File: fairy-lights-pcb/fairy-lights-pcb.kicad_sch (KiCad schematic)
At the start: 5 parts, among them J1 Barrel_Jack_MountingPin, J2 Conn_LED_Strand, U1 WeMos_D1_mini, U2 TXS0108EPW

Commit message: Add board design and missing component footprints
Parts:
- J2: footprint (none) -> Connector_PinHeader_2.54mm:PinHeader_1x04_P2.54mm_Vertical
- R1: footprint (none) -> Resistor_THT:R_Axial_DIN0204_L3.6mm_D1.6mm_P7.62mm_Horizontal
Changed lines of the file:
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@@
 			)
 		)
-		(property "Footprint" ""
+		(property "Footprint" "Connector_PinHeader_2.54mm:PinHeader_1x04_P2.54mm_Vertical"
 			(at 179.07 75.057 0)
 			(effects
@@
 			)
 		)
-		(property "Footprint" ""
+		(property "Footprint" "Resistor_THT:R_Axial_DIN0204_L3.6mm_D1.6mm_P7.62mm_Horizontal"
 			(at 129.54 60.198 90)
 			(effects

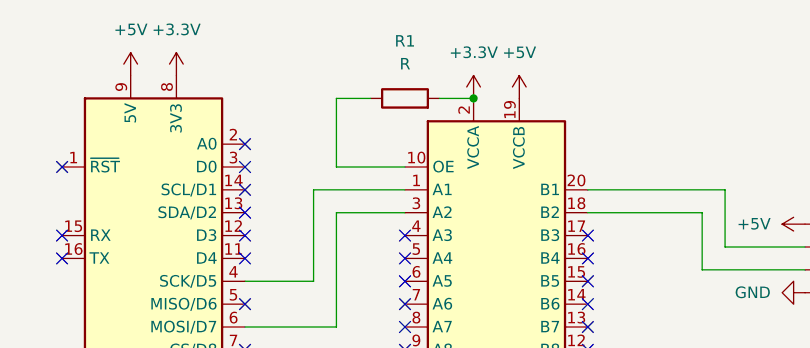
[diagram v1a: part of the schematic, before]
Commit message: Add resistor value and connector annotations
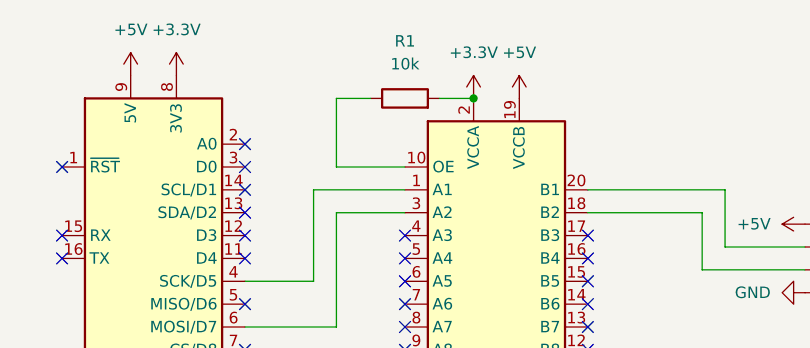
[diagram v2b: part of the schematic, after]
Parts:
- R1: value R -> 10k
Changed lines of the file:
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@@
 			)
 		)
-		(property "Value" "R"
+		(property "Value" "10k"
 			(at 129.54 54.61 90)
 			(effects

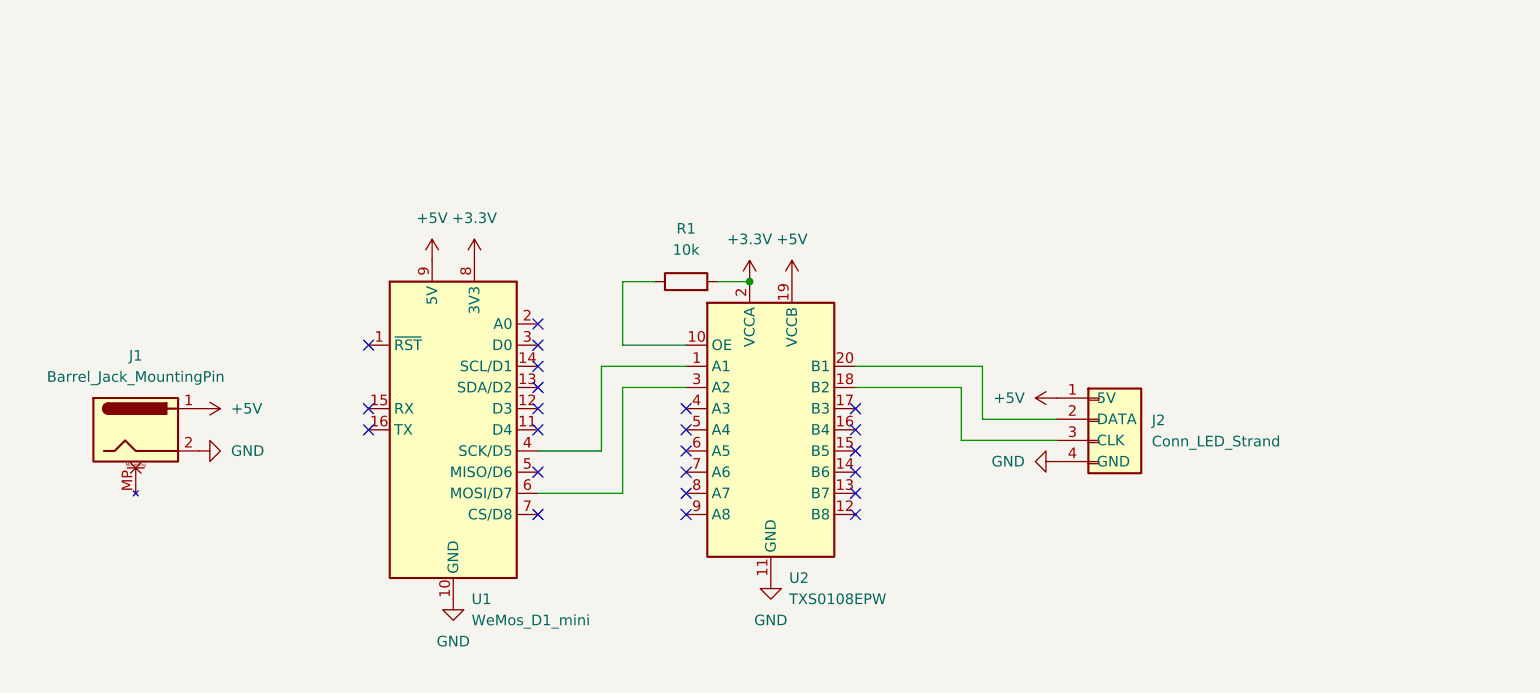
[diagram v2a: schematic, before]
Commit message: Add more stuff
- Two more output headers (functionally identical but one labeled like
  the first LED one and the second generically)
- Header for a power switch (interposed between the power jack and the
  5V rail)
- Header for a user switch/button (from a GPIO pin to ground)
- User LED (from a GPIO pin to ground)
- Miscellaneous header (exposing all other pins of the microcontroller)
- Mounting holes
- Shifted power jack closer to PCB edge
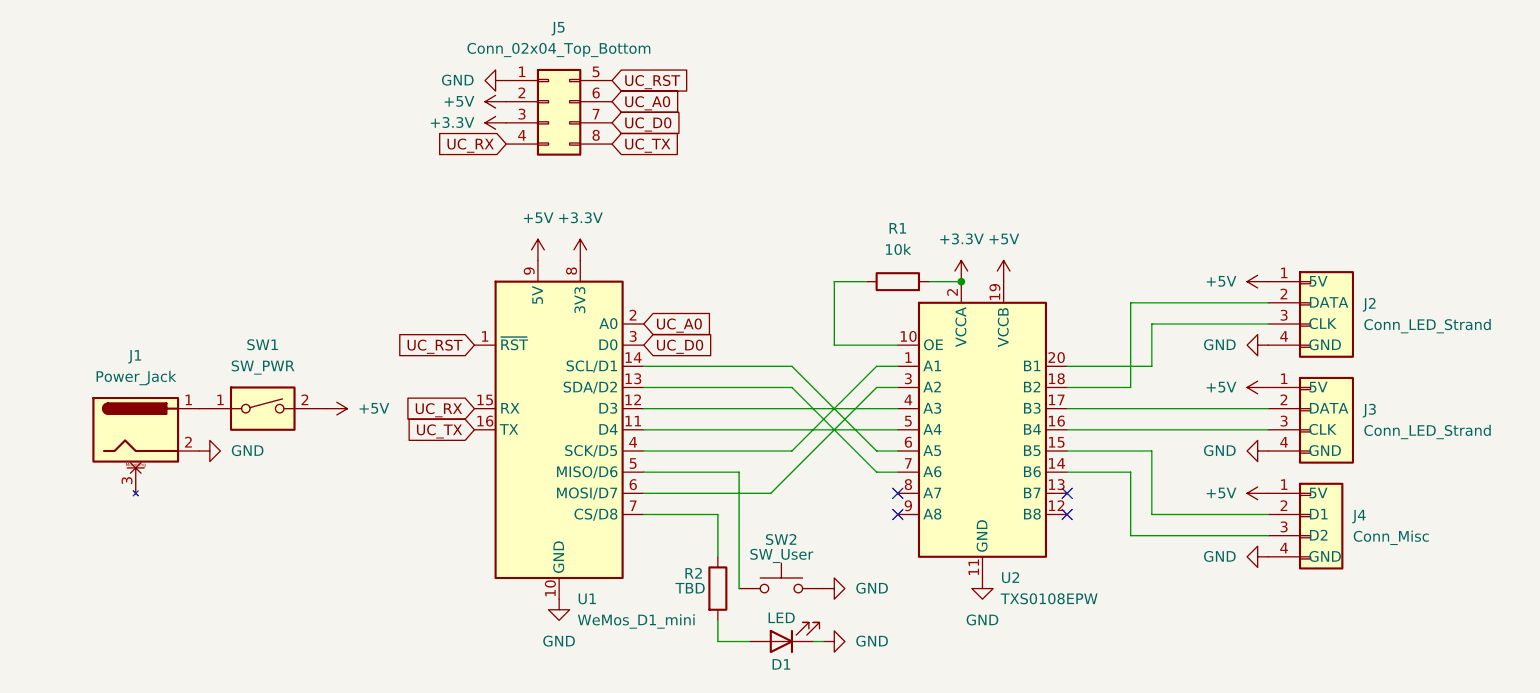
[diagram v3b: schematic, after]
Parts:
- added D1: LED, LED_THT:LED_D3.0mm, symbol Device:LED
- added J3: Conn_LED_Strand, Connector_PinHeader_2.54mm:PinHeader_1x04_P2.54mm_Vertical, symbol CustomSymbols:Conn_LED_Strand
- added J4: Conn_Misc, Connector_PinHeader_2.54mm:PinHeader_1x04_P2.54mm_Vertical, symbol CustomSymbols:Conn_Misc
- added J5: Conn_02x04_Top_Bottom, Connector_PinHeader_2.54mm:PinHeader_2x04_P2.54mm_Vertical, symbol Connector_Generic:Conn_02x04_Top_Bottom
- added R2: TBD, Resistor_THT:R_Axial_DIN0204_L3.6mm_D1.6mm_P7.62mm_Horizontal, symbol Device:R
- added SW1: SW_PWR, Connector_PinHeader_2.54mm:PinHeader_1x02_P2.54mm_Vertical, symbol CustomSymbols:SW_PWR
- added SW2: SW_User, Connector_PinHeader_2.54mm:PinHeader_1x02_P2.54mm_Vertical, symbol Switch:SW_Push
- J1: value Barrel_Jack_MountingPin -> Power_Jack
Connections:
- net +3.3V: now also J5.3 (Pin_3)
- net +5V: now also J3.1 (5V), J4.1 (5V), J5.2 (Pin_2), SW1.2; no longer J1.1
- net GND: now also D1.1 (K), J3.4 (GND), J4.4 (GND), J5.1 (Pin_1), SW2.2
- net at J2.2 (DATA): now also U2.18 (B2); no longer U2.20 (B1)
- net at J2.3 (CLK): now also U2.20 (B1); no longer U2.18 (B2)
- net at U2.14 (B6): now also J4.3 (D2)
- net at U2.15 (B5): now also J4.2 (D1)
- net at U2.16 (B4): now also J3.3 (CLK)
- net at U2.17 (B3): now also J3.2 (DATA)
- net at U2.4 (A3): now also U1.12 (D3)
- net at U2.5 (A4): now also U1.11 (D4)
- net at U2.6 (A5): now also U1.14 (SCL/D1)
- net at U2.7 (A6): now also U1.13 (SDA/D2)
- net UC_RST: now reaches U1.1 (~{RST})
- net UC_RST: now also J5.5 (Pin_5)
- net UC_RX: now reaches U1.15 (RX)
- net UC_RX: now also J5.4 (Pin_4)
- net UC_TX: now reaches U1.16 (TX)
- net UC_TX: now also J5.8 (Pin_8)
- net UC_A0: now reaches U1.2 (A0)
- net UC_A0: now also J5.6 (Pin_6)
- net UC_D0: now reaches U1.3 (D0)
- net UC_D0: now also J5.7 (Pin_7)
- net at U1.5 (MISO/D6): now also SW2.1
- net at U1.7 (CS/D8): now also R2.1
- new net: D1.2 (A), R2.2
- new net: J1.1, SW1.1
- no-connect marks 23 -> 4
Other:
- moved on the sheet: J2, R1, U1, U2

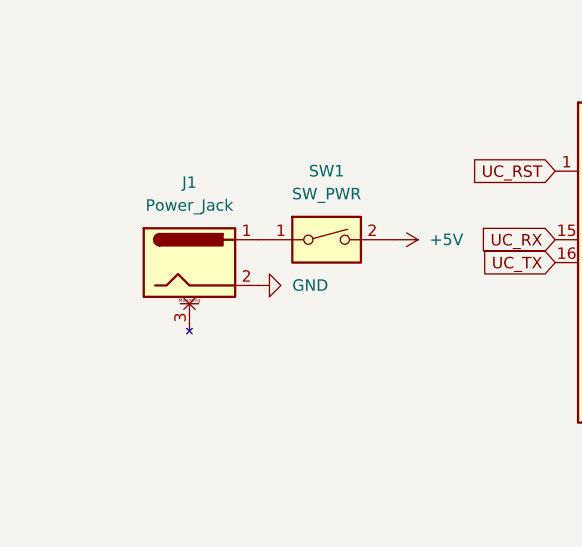
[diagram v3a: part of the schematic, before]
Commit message: Increase thickness of 5V traces
Also redoes all routing, because why not.
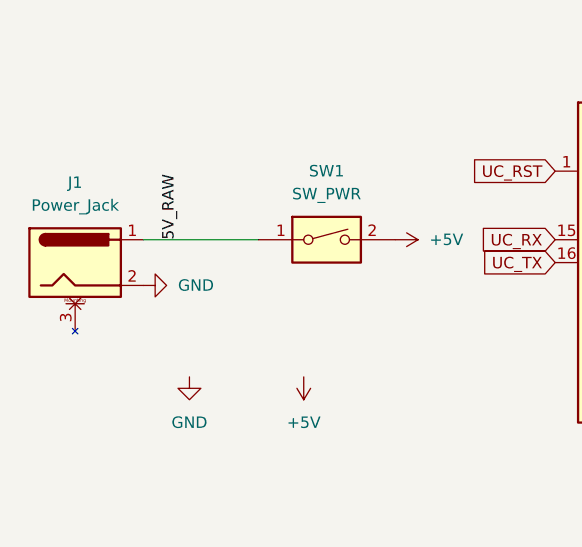
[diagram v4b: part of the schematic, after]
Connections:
- net 5V_RAW: now reaches J1.1, SW1.1
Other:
- moved on the sheet: J1
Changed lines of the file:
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@@
+	(wire
+		(pts
+			(xy 58.42 73.66) (xy 71.12 73.66)
+		)
+		(stroke
+			(width 0)
+			(type default)
+		)
+	)
 	(wire
 		(pts
@@
 		)
 	)
+	(label "5V_RAW"
+		(at 62.23 73.66 90)
+		(fields_autoplaced yes)
+		(effects
+			(font
+				(size 1.27 1.27)
+			)
+			(justify left bottom)
+		)
+	)
 	(global_label "UC_D0"
 		(shape input)
@@
 		)
 	)
+	(netclass_flag ""
+		(length 2.54)
+		(shape round)
+		(at 63.5 88.9 0)
+		(fields_autoplaced yes)
+		(effects
+			(font
+				(size 1.27 1.27)
+			)
+			(justify left bottom)
+		)
+		(property "Netclass" "Power"
+			(at 64.1985 86.36 0)
+			(effects
+				(font
+					(size 1.27 1.27)
+					(italic yes)
+				)
+				(justify left)
+			)
+		)
+	)
+	(netclass_flag ""
+		(length 2.54)
+		(shape round)
+		(at 64.77 73.66 0)
+		(fields_autoplaced yes)
+		(effects
+			(font
+				(size 1.27 1.27)
+			)
+			(justify left bottom)
+		)
+		(property "Netclass" "Power"
+			(at 65.4685 71.12 0)
+			(effects
+				(font
+					(size 1.27 1.27)
+					(italic yes)
+				)
+				(justify left)
+			)
+		)
+	)
+	(netclass_flag ""
+		(length 2.54)
+		(shape round)
+		(at 76.2 88.9 0)
+		(fields_autoplaced yes)
+		(effects
+			(font
+				(size 1.27 1.27)
+			)
+			(justify left bottom)
+		)
+		(property "Netclass" "Power"
+			(at 76.8985 86.36 0)
+			(effects
+				(font
+					(size 1.27 1.27)
+					(italic yes)
+				)
+				(justify left)
+			)
+		)
+	)
 	(symbol
 		(lib_id "Switch:SW_Push")
@@
 	)
 	(symbol
+		(lib_id "power:GND")
+		(at 63.5 88.9 0)
+		(unit 1)
+		(exclude_from_sim no)
+		(in_bom yes)
+		(on_board yes)
+		(dnp no)
+		(fields_autoplaced yes)
+		(property "Reference" "#PWR021"
+			(at 63.5 95.25 0)
+			(effects
+				(font
+					(size 1.27 1.27)
+				)
+				(hide yes)
+			)
+		)
+		(property "Value" "GND"
+			(at 63.5 93.98 0)
+			(effects
+				(font
+					(size 1.27 1.27)
+				)
+			)
+		)
+		(property "Footprint" ""
+			(at 63.5 88.9 0)
+			(effects
+				(font
+					(size 1.27 1.27)
+				)
+				(hide yes)
+			)
+		)
+		(property "Datasheet" ""
+			(at 63.5 88.9 0)
+			(effects
+				(font
+					(size 1.27 1.27)
+				)
+				(hide yes)
+			)
+		)
+		(property "Description" "Power symbol creates a global label with name \"GND\" , ground"
+			(at 63.5 88.9 0)
+			(effects
+				(font
+					(size 1.27 1.27)
+				)
+				(hide yes)
+			)
+		)
+		(pin "1"
+		)
+		(instances
+			(project "fairy-lights-pcb"
+				(path "/c40a4c0f-dcaf-41c4-b21e-10b233cddaa8"
+					(reference "#PWR021")
+					(unit 1)
+				)
+			)
+		)
+	)
+	(symbol
 		(lib_id "power:+5V")
 		(at 199.39 71.12 90)
@@
 	(symbol
 		(lib_id "CustomSymbols:Power_Jack")
-		(at 63.5 76.2 0)
+		(at 50.8 76.2 0)
 		(unit 1)
 		(exclude_from_sim no)
@@
 		(fields_autoplaced yes)
 		(property "Reference" "J1"
-			(at 63.5 67.31 0)
+			(at 50.8 67.31 0)
 			(effects
 				(font
@@
 		)
 		(property "Value" "Power_Jack"
-			(at 63.5 69.85 0)
+			(at 50.8 69.85 0)
 			(effects
 				(font
@@
 		)
 		(property "Footprint" "Connector_BarrelJack:BarrelJack_Horizontal"
-			(at 64.77 77.216 0)
+			(at 52.07 77.216 0)
 			(effects
 				(font
@@
 		)
 		(property "Datasheet" "~"
-			(at 64.77 77.216 0)
+			(at 52.07 77.216 0)
 			(effects
 				(font
@@
 		)
 		(property "Description" "Power_Jack"
-			(at 63.5 76.2 0)
+			(at 50.8 76.2 0)
 			(effects
 				(font
@@
 	)
 	(symbol
+		(lib_id "power:+5V")
+		(at 76.2 88.9 180)
+		(unit 1)
+		(exclude_from_sim no)
+		(in_bom yes)
+		(on_board yes)
+		(dnp no)
+		(fields_autoplaced yes)
+		(property "Reference" "#PWR020"
+			(at 76.2 85.09 0)
+			(effects
+				(font
+					(size 1.27 1.27)
+				)
+				(hide yes)
+			)
+		)
+		(property "Value" "+5V"
+			(at 76.2 93.98 0)
+			(effects
+				(font
+					(size 1.27 1.27)
+				)
+			)
+		)
+		(property "Footprint" ""
+			(at 76.2 88.9 0)
+			(effects
+				(font
+					(size 1.27 1.27)
+				)
+				(hide yes)
+			)
+		)
+		(property "Datasheet" ""
+			(at 76.2 88.9 0)
+			(effects
+				(font
+					(size 1.27 1.27)
+				)
+				(hide yes)
+			)
+		)
+		(property "Description" "Power symbol creates a global label with name \"+5V\""
+			(at 76.2 88.9 0)
+			(effects
+				(font
+					(size 1.27 1.27)
+				)
+				(hide yes)
+			)
+		)
+		(pin "1"
+		)
+		(instances
+			(project ""
+				(path "/c40a4c0f-dcaf-41c4-b21e-10b233cddaa8"
+					(reference "#PWR020")
+					(unit 1)
+				)
+			)
+		)
+	)
+	(symbol
 		(lib_id "power:GND")
 		(at 199.39 66.04 270)
@@
 	(symbol
 		(lib_id "power:GND")
-		(at 71.12 78.74 90)
+		(at 58.42 78.74 90)
 		(unit 1)
 		(exclude_from_sim no)
@@
 		(fields_autoplaced yes)
 		(property "Reference" "#PWR01"
-			(at 77.47 78.74 0)
+			(at 64.77 78.74 0)
 			(effects
 				(font
@@
 		)
 		(property "Value" "GND"
-			(at 74.93 78.7399 90)
+			(at 62.23 78.7399 90)
 			(effects
 				(font
@@
 		)
 		(property "Footprint" ""
-			(at 71.12 78.74 0)
+			(at 58.42 78.74 0)
 			(effects
 				(font
@@
 		)
 		(property "Datasheet" ""
-			(at 71.12 78.74 0)
+			(at 58.42 78.74 0)
 			(effects
 				(font
@@
 		)
 		(property "Description" "Power symbol creates a global label with name \"GND\" , ground"
-			(at 71.12 78.74 0)
-			(effects
-				(font
+			(at 58.42 78.74 0)
+			(effects
+				(font

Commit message: Add mounting holes to schematic
This should mollify the design rule checker.
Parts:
- added H1, H2, H3, H4: MountingHole, MountingHole:MountingHole_2.2mm_M2, symbol Mechanical:MountingHole

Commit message: Connect barrel jack mounting pin to ground
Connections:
- net GND: now also J1.3 (MP)
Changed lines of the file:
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@@
+	)
+	(symbol
+		(lib_id "power:GND")
+		(at 50.8 83.82 0)
+		(unit 1)
+		(exclude_from_sim no)
+		(in_bom yes)
+		(on_board yes)
+		(dnp no)
+		(fields_autoplaced yes)
+		(property "Reference" "#PWR022"
+			(at 50.8 90.17 0)
+			(effects
+				(font
+					(size 1.27 1.27)
+				)
+				(hide yes)
+			)
+		)
+		(property "Value" "GND"
+			(at 50.8 88.9 0)
+			(effects
+				(font
+					(size 1.27 1.27)
+				)
+			)
+		)
+		(property "Footprint" ""
+			(at 50.8 83.82 0)
+			(effects
+				(font
+					(size 1.27 1.27)
+				)
+				(hide yes)
+			)
+		)
+		(property "Datasheet" ""
+			(at 50.8 83.82 0)
+			(effects
+				(font
+					(size 1.27 1.27)
+				)
+				(hide yes)
+			)
+		)
+		(property "Description" "Power symbol creates a global label with name \"GND\" , ground"
+			(at 50.8 83.82 0)
+			(effects
+				(font
+					(size 1.27 1.27)
+				)
+				(hide yes)
+			)
+		)
+		(pin "1"
+		)
+		(instances
+			(project "fairy-lights-pcb"
+				(path "/c40a4c0f-dcaf-41c4-b21e-10b233cddaa8"
+					(reference "#PWR022")
+					(unit 1)
+				)
+			)
+		)
 	)
 	(symbol

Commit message: Update user LED resistor value
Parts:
- R2: value TBD -> 47
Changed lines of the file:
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@@
 		(dnp no)
 		(property "Reference" "R2"
-			(at 129.286 93.472 0)
+			(at 132.08 93.472 0)
 			(effects
 				(font
 					(size 1.27 1.27)
 				)
-				(justify left)
+				(justify right)
 			)
 		)
-		(property "Value" "TBD"
-			(at 128.27 95.25 0)
+		(property "Value" "47"
+			(at 132.08 95.25 0)
 			(effects
 				(font
 					(size 1.27 1.27)
 				)
-				(justify left)
+				(justify right)
 			)
 		)
